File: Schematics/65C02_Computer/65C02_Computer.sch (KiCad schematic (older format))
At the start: 33 parts

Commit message: Various updates to schematic
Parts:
- added unit 5 of U1
- added unit 5 of U4
- added unit 3 of U5
- J2: renamed from J?; value Conn_02x16_Top_Bottom -> Expansion port; symbol Connector_Generic:Conn_02x16_Top_Bottom -> Connector_Generic:Conn_02x16_Odd_Even
- U4: renamed from U?; footprint (none) -> Package_DIP:DIP-14_W7.62mm_Socket
- gave numbers to parts that had none: 29
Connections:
- net +5V: now also U1.14 (VCC), U4.14 (VCC), U5.14 (VCC)
- net CLK: now also J2.18 (Pin_18); no longer J2.25 (Pin_25)
- net GND: now also J2.30 (Pin_30), U1.7 (GND), U4.7 (GND), U5.7 (GND); no longer J2.31 (Pin_31)
- net R~W: now also J2.20 (Pin_20); no longer J2.26 (Pin_26)
- net a1: now also J2.3 (Pin_3); no longer J2.2 (Pin_2)
- net a10: now also J2.21 (Pin_21); no longer J2.11 (Pin_11)
- net a11: now also J2.23 (Pin_23); no longer J2.12 (Pin_12)
- net a12: now also J2.25 (Pin_25); no longer J2.13 (Pin_13)
- net a13: now also J2.27 (Pin_27); no longer J2.14 (Pin_14)
- net a14: now also J2.29 (Pin_29); no longer J2.15 (Pin_15)
- net a15: now also J2.31 (Pin_31); no longer J2.16 (Pin_16)
- net a2: now also J2.5 (Pin_5); no longer J2.3 (Pin_3)
- net a3: now also J2.7 (Pin_7); no longer J2.4 (Pin_4)
- net a4: now also J2.9 (Pin_9); no longer J2.5 (Pin_5)
- net a5: now also J2.11 (Pin_11); no longer J2.6 (Pin_6)
- net a6: now also J2.13 (Pin_13); no longer J2.7 (Pin_7)
- net a7: now also J2.15 (Pin_15); no longer J2.8 (Pin_8)
- net a8: now also J2.17 (Pin_17); no longer J2.9 (Pin_9)
- net a9: now also J2.19 (Pin_19); no longer J2.10 (Pin_10)
- net d0: now also J2.2 (Pin_2); no longer J2.17 (Pin_17)
- net d1: now also J2.4 (Pin_4); no longer J2.18 (Pin_18)
- net d2: now also J2.6 (Pin_6); no longer J2.19 (Pin_19)
- net d3: now also J2.8 (Pin_8); no longer J2.20 (Pin_20)
- net d4: now also J2.10 (Pin_10); no longer J2.21 (Pin_21)
- net d5: now also J2.12 (Pin_12); no longer J2.22 (Pin_22)
- net d6: now also J2.14 (Pin_14); no longer J2.23 (Pin_23)
- net d7: now also J2.16 (Pin_16); no longer J2.24 (Pin_24)
- net ~IOCS: now also J2.22 (Pin_22); no longer J2.27 (Pin_27)
- net ~IRQX: now also J2.26 (Pin_26); no longer J2.29 (Pin_29)
- net ~RES: now also J2.24 (Pin_24); no longer J2.28 (Pin_28)
- no-connect marks 6 -> 7

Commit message: Further updates to schematic
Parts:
- added R13: 4K7, Resistor_THT:R_Axial_DIN0207_L6.3mm_D2.5mm_P7.62mm_Horizontal, symbol Device:R
- R1, R2, R4: value 3K3 -> 4K7
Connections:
- net +5V: now also R13.1
- net ~AIRQ: now also R13.2
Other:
- moved on the sheet: R4, U5A
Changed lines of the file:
@@
 P 1000 1600
 F 0 "R2" V 900 1600 50  0000 C CNN
-F 1 "3K3" V 1000 1600 50  0000 C CNN
+F 1 "4K7" V 1000 1600 50  0000 C CNN
 F 2 "Resistor_THT:R_Axial_DIN0207_L6.3mm_D2.5mm_P7.62mm_Horizontal" V 930 1600 50  0001 C CNN
 F 3 "~" H 1000 1600 50  0001 C CNN
@@
 P 1000 1200
 F 0 "R1" V 900 1200 50  0000 C CNN
-F 1 "3K3" V 1000 1200 50  0000 C CNN
+F 1 "4K7" V 1000 1200 50  0000 C CNN
 F 2 "Resistor_THT:R_Axial_DIN0207_L6.3mm_D2.5mm_P7.62mm_Horizontal" V 930 1200 50  0001 C CNN
 F 3 "~" H 1000 1200 50  0001 C CNN
@@
 L 74xx:74LS21 U5
 U 1 1 5E23A6D1
-P 8450 5300
-F 0 "U5" H 8450 5675 50  0000 C CNN
-F 1 "74HC21" H 8450 5584 50  0000 C CNN
-F 2 "Package_DIP:DIP-14_W7.62mm_Socket" H 8450 5300 50  0001 C CNN
-F 3 "http://www.ti.com/lit/gpn/sn74LS21" H 8450 5300 50  0001 C CNN
-	1    8450 5300
-	1    0    0    -1
-$EndComp
-Text GLabel 8050 5050 1    50   Input ~ 0
+P 9000 5400
+F 0 "U5" H 9000 5775 50  0000 C CNN
+F 1 "74HC21" H 9000 5684 50  0000 C CNN
+F 2 "Package_DIP:DIP-14_W7.62mm_Socket" H 9000 5400 50  0001 C CNN
+F 3 "http://www.ti.com/lit/gpn/sn74LS21" H 9000 5400 50  0001 C CNN
+	1    9000 5400
+	1    0    0    -1
+$EndComp
+Text GLabel 8600 5050 1    50   Input ~ 0
 ~V1IRQ
-Text GLabel 7900 5050 1    50   Input ~ 0
+Text GLabel 8450 5050 1    50   Input ~ 0
 ~V2IRQ
-Text GLabel 7750 5050 1    50   Input ~ 0
+Text GLabel 8300 5050 1    50   Input ~ 0
 ~AIRQ
 Wire Wire Line
-	8050 5050 8050 5150
-Wire Wire Line
-	8050 5150 8150 5150
-Wire Wire Line
-	7900 5050 7900 5250
-Wire Wire Line
-	7900 5250 8150 5250
-Wire Wire Line
-	7750 5050 7750 5350
-Wire Wire Line
-	7750 5350 8150 5350
-Wire Wire Line
-	7600 5050 7600 5450
-Wire Wire Line
-	7600 5450 8150 5450
-Text GLabel 8850 5300 2    50   Output ~ 0
+	8600 5050 8600 5250
+Wire Wire Line
+	8600 5250 8700 5250
+Wire Wire Line
+	8450 5050 8450 5350
+Wire Wire Line
+	8450 5350 8700 5350
+Wire Wire Line
+	8300 5050 8300 5450
+Wire Wire Line
+	8300 5450 8700 5450
+Wire Wire Line
+	8000 5050 8000 5550
+Text GLabel 9400 5400 2    50   Output ~ 0
 ~IRQ
 Wire Wire Line
-	8750 5300 8850 5300
+	9300 5400 9400 5400
 Wire Wire Line
 	2300 1300 2850 1300
@@
 Wire Wire Line
 	7150 5550 7150 5050
-Text GLabel 7600 5050 1    50   Input ~ 0
+Text GLabel 8000 5050 1    50   Input ~ 0
 ~IRQX
-Text GLabel 7450 5050 1    50   Input ~ 0
+Text GLabel 7850 5050 1    50   Input ~ 0
 +5V
 $Comp
 L Device:R R4
 U 1 1 5E451554
-P 7450 5300
-F 0 "R4" V 7350 5300 50  0000 C CNN
-F 1 "3K3" V 7450 5300 50  0000 C CNN
-F 2 "Resistor_THT:R_Axial_DIN0207_L6.3mm_D2.5mm_P7.62mm_Horizontal" V 7380 5300 50  0001 C CNN
-F 3 "~" H 7450 5300 50  0001 C CNN
-	1    7450 5300
-	1    0    0    -1
-$EndComp
-Wire Wire Line
-	7450 5050 7450 5150
-Wire Wire Line
-	7450 5450 7600 5450
-Connection ~ 7600 5450
+P 7850 5300
+F 0 "R4" V 7750 5300 50  0000 C CNN
+F 1 "4K7" V 7850 5300 50  0000 C CNN
+F 2 "Resistor_THT:R_Axial_DIN0207_L6.3mm_D2.5mm_P7.62mm_Horizontal" V 7780 5300 50  0001 C CNN
+F 3 "~" H 7850 5300 50  0001 C CNN
+	1    7850 5300
+	1    0    0    -1
+$EndComp
+Wire Wire Line
+	7850 5050 7850 5150
 $Comp
 L Connector:Conn_01x02_Male J1
@@
 Wire Wire Line
 	2850 6350 2850 6250
+Text GLabel 8150 5050 1    50   Input ~ 0
++5V
+$Comp
+L Device:R R13
+U 1 1 5E47EC64
+P 8150 5300
+F 0 "R13" V 8050 5300 50  0000 C CNN
+F 1 "4K7" V 8150 5300 50  0000 C CNN
+F 2 "Resistor_THT:R_Axial_DIN0207_L6.3mm_D2.5mm_P7.62mm_Horizontal" V 8080 5300 50  0001 C CNN
+F 3 "~" H 8150 5300 50  0001 C CNN
+	1    8150 5300
+	1    0    0    -1
+$EndComp
+Wire Wire Line
+	8150 5050 8150 5150
+Wire Wire Line
+	8000 5550 8700 5550
+Wire Wire Line
+	7850 5450 7850 5550
+Wire Wire Line
+	7850 5550 8000 5550
+Connection ~ 8000 5550
+Wire Wire Line
+	8150 5450 8300 5450
+Connection ~ 8300 5450
 Wire Bus Line
 	3100 5450 3100 5650

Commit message: Reordered PCB components
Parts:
- J1: footprint Connector_PinHeader_2.54mm:PinHeader_1x02_P2.54mm_Vertical -> Connector_PinHeader_2.54mm:PinHeader_1x03_P2.54mm_Vertical; symbol Connector:Conn_01x02_Male -> Connector:Conn_01x03_Male
- renumbered C9 to C1, C1 to C11, C3 to C12, C5 to C13, C7 to C14, C11 to C15, C12 to C16, C6 to C2, C13 to C3, C2 to C5, C8 to C6, C10 to C7, R3 to R1, R4 to R13, R5 to R2, R6 to R3, R13 to R6, R1 to R7, R2 to R8, U5 to U1, U4 to U2, U1 to U3, U7 to U4, U3 to U7, U2 to U8, U6 to U9
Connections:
- net CLK: now also J1.2 (Pin_2); no longer J1.1 (Pin_1)
- net CLKOUT: now also J1.3 (Pin_3); no longer J1.2 (Pin_2)
- net GND: now also J1.1 (Pin_1)
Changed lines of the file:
@@
 	4400 1300 4500 1300
 $Comp
-L 74xx:74HC02 U1
+L 74xx:74HC02 U3
 U 2 1 5E1744DD
 P 4000 2000
-F 0 "U1" H 4000 2325 50  0000 C CNN
+F 0 "U3" H 4000 2325 50  0000 C CNN
 F 1 "74HC02" H 4000 2234 50  0000 C CNN
 F 2 "Package_DIP:DIP-14_W7.62mm_Socket" H 4000 2000 50  0001 C CNN
@@
 $EndComp
 $Comp
-L 74xx:74HC00 U4
+L 74xx:74HC00 U2
 U 3 1 5E171DC1
 P 4800 2100
-F 0 "U4" H 4800 2425 50  0000 C CNN
+F 0 "U2" H 4800 2425 50  0000 C CNN
 F 1 "74HC00" H 4800 2334 50  0000 C CNN
 F 2 "Package_DIP:DIP-14_W7.62mm_Socket" H 4800 2100 50  0001 C CNN
@@
 $EndComp
 $Comp
-L 74xx:74HC00 U4
+L 74xx:74HC00 U2
 U 2 1 5E16FD0A
 P 4800 1400
-F 0 "U4" H 4800 1725 50  0000 C CNN
+F 0 "U2" H 4800 1725 50  0000 C CNN
 F 1 "74HC00" H 4800 1634 50  0000 C CNN
 F 2 "Package_DIP:DIP-14_W7.62mm_Socket" H 4800 1400 50  0001 C CNN
@@
 $EndComp
 $Comp
-L 74xx:74HC00 U4
+L 74xx:74HC00 U2
 U 1 1 5E16D50B
 P 4000 1300
-F 0 "U4" H 4000 1625 50  0000 C CNN
+F 0 "U2" H 4000 1625 50  0000 C CNN
 F 1 "74HC00" H 4000 1534 50  0000 C CNN
 F 2 "Package_DIP:DIP-14_W7.62mm_Socket" H 4000 1300 50  0001 C CNN
@@
 $EndComp
 $Comp
-L Device:C C13
+L Device:C C3
 U 1 1 5E15B54A
 P 10150 3350
-F 0 "C13" H 10265 3396 50  0000 L CNN
+F 0 "C3" H 10265 3396 50  0000 L CNN
 F 1 "0.1uF" H 10265 3305 50  0000 L CNN
 F 2 "Capacitor_THT:C_Disc_D3.4mm_W2.1mm_P2.50mm" H 10188 3200 50  0001 C CNN
@@
 $EndComp
 $Comp
-L Device:R R2
+L Device:R R8
 U 1 1 5E14ABB7
 P 1000 1600
-F 0 "R2" V 900 1600 50  0000 C CNN
+F 0 "R8" V 900 1600 50  0000 C CNN
 F 1 "4K7" V 1000 1600 50  0000 C CNN
 F 2 "Resistor_THT:R_Axial_DIN0207_L6.3mm_D2.5mm_P7.62mm_Horizontal" V 930 1600 50  0001 C CNN
@@
 $EndComp
 $Comp
-L Device:R R1
+L Device:R R7
 U 1 1 5E14A45B
 P 1000 1200
-F 0 "R1" V 900 1200 50  0000 C CNN
+F 0 "R7" V 900 1200 50  0000 C CNN
 F 1 "4K7" V 1000 1200 50  0000 C CNN
 F 2 "Resistor_THT:R_Axial_DIN0207_L6.3mm_D2.5mm_P7.62mm_Horizontal" V 930 1200 50  0001 C CNN
@@
 $EndComp
 $Comp
-L 6502:65C02S U3
+L 6502:65C02S U7
 U 1 1 5E135500
 P 1800 2000
-F 0 "U3" H 1800 3150 50  0000 C CNN
+F 0 "U7" H 1800 3150 50  0000 C CNN
 F 1 "65C02S" H 1800 3050 50  0000 C CNN
 F 2 "Package_DIP:DIP-40_W15.24mm_Socket" H 1650 2950 50  0001 C CNN
@@
 $EndComp
 $Comp
-L 6502:28C256 U2
+L 6502:28C256 U8
 U 1 1 5E3D4005
 P 1550 5000
-F 0 "U2" H 1550 5915 50  0000 C CNN
+F 0 "U8" H 1550 5915 50  0000 C CNN
 F 1 "28C256" H 1550 5824 50  0000 C CNN
 F 2 "Package_DIP:DIP-28_W15.24mm_Socket" H 1500 5800 50  0001 C CNN
@@
 	2600 5050 2700 5150
 $Comp
-L 6502:62256 U6
+L 6502:62256 U9
 U 1 1 5E37B16A
 P 3850 5000
-F 0 "U6" H 3850 5915 50  0000 C CNN
+F 0 "U9" H 3850 5915 50  0000 C CNN
 F 1 "62256" H 3850 5824 50  0000 C CNN
 F 2 "Package_DIP:DIP-28_W15.24mm_Socket" H 3800 5800 50  0001 C CNN
@@
 	4350 4450 4600 4450
 $Comp
-L Timer:NE555 U7
+L Timer:NE555 U4
 U 1 1 5E17C676
 P 7450 1700
-F 0 "U7" H 7450 1750 50  0000 C CNN
+F 0 "U4" H 7450 1750 50  0000 C CNN
 F 1 "NE555" H 7450 1650 50  0000 C CNN
 F 2 "Package_DIP:DIP-8_W7.62mm_Socket" H 7450 1700 50  0001 C CNN
@@
 	8050 1900 7950 1900
 $Comp
-L Device:R R5
+L Device:R R2
 U 1 1 5E1F5B26
 P 8050 1250
-F 0 "R5" V 7950 1250 50  0000 C CNN
+F 0 "R2" V 7950 1250 50  0000 C CNN
 F 1 "47K" V 8050 1250 50  0000 C CNN
 F 2 "Resistor_THT:R_Axial_DIN0207_L6.3mm_D2.5mm_P7.62mm_Horizontal" V 7980 1250 50  0001 C CNN
@@
 $EndComp
 $Comp
-L Device:CP C8
+L Device:CP C6
 U 1 1 5E2337BD
 P 8050 2150
-F 0 "C8" H 8168 2196 50  0000 L CNN
+F 0 "C6" H 8168 2196 50  0000 L CNN
 F 1 "10uF" H 8168 2105 50  0000 L CNN
 F 2 "Capacitor_THT:CP_Radial_D5.0mm_P2.50mm" H 8088 2000 50  0001 C CNN
@@
 Connection ~ 6700 1500
 $Comp
-L Device:R R3
+L Device:R R1
 U 1 1 5E3A85D8
 P 6700 1250
-F 0 "R3" V 6600 1250 50  0000 C CNN
+F 0 "R1" V 6600 1250 50  0000 C CNN
 F 1 "1M" V 6700 1250 50  0000 C CNN
 F 2 "Resistor_THT:R_Axial_DIN0207_L6.3mm_D2.5mm_P7.62mm_Horizontal" V 6630 1250 50  0001 C CNN
@@
 	8850 1500 8950 1500
 $Comp
-L Device:R R6
+L Device:R R3
 U 1 1 5E552FBE
 P 8950 1250
-F 0 "R6" V 8850 1250 50  0000 C CNN
+F 0 "R3" V 8850 1250 50  0000 C CNN
 F 1 "1K" V 8950 1250 50  0000 C CNN
 F 2 "Resistor_THT:R_Axial_DIN0207_L6.3mm_D2.5mm_P7.62mm_Horizontal" V 8880 1250 50  0001 C CNN
@@
 GND
 $Comp
-L Device:C C2
+L Device:C C5
 U 1 1 5E7C431C
 P 6150 1700
-F 0 "C2" H 6265 1746 50  0000 L CNN
+F 0 "C5" H 6265 1746 50  0000 L CNN
 F 1 "0.1uF" H 6265 1655 50  0000 L CNN
 F 2 "Capacitor_THT:C_Disc_D3.4mm_W2.1mm_P2.50mm" H 6188 1550 50  0001 C CNN
@@
 	2850 1500 2850 1300
 $Comp
-L 74xx:74HC00 U4
+L 74xx:74HC00 U2
 U 4 1 5E218D59
 P 8550 1500
-F 0 "U4" H 8550 1825 50  0000 C CNN
+F 0 "U2" H 8550 1825 50  0000 C CNN
 F 1 "74HC00" H 8550 1734 50  0000 C CNN
 F 2 "Package_DIP:DIP-14_W7.62mm_Socket" H 8550 1500 50  0001 C CNN
@@
 	8150 1500 8150 1600
 $Comp
-L 74xx:74LS21 U5
+L 74xx:74LS21 U1
 U 1 1 5E23A6D1
 P 9000 5400
-F 0 "U5" H 9000 5775 50  0000 C CNN
+F 0 "U1" H 9000 5775 50  0000 C CNN
 F 1 "74HC21" H 9000 5684 50  0000 C CNN
 F 2 "Package_DIP:DIP-14_W7.62mm_Socket" H 9000 5400 50  0001 C CNN
@@
 	2850 1300 2850 1000
 $Comp
-L Device:C C12
+L Device:C C16
 U 1 1 5E3E0FFB
 P 9700 3350
-F 0 "C12" H 9815 3396 50  0000 L CNN
+F 0 "C16" H 9815 3396 50  0000 L CNN
 F 1 "0.1uF" H 9815 3305 50  0000 L CNN
 F 2 "Capacitor_THT:C_Disc_D3.4mm_W2.1mm_P2.50mm" H 9738 3200 50  0001 C CNN
@@
 $EndComp
 $Comp
-L Device:C C11
+L Device:C C15
 U 1 1 5E3E14F5
 P 9250 3350
-F 0 "C11" H 9365 3396 50  0000 L CNN
+F 0 "C15" H 9365 3396 50  0000 L CNN
 F 1 "0.1uF" H 9365 3305 50  0000 L CNN
 F 2 "Capacitor_THT:C_Disc_D3.4mm_W2.1mm_P2.50mm" H 9288 3200 50  0001 C CNN
@@
 $EndComp
 $Comp
-L Device:C C10
+L Device:C C7
 U 1 1 5E3E1910
 P 8800 3350
-F 0 "C10" H 8915 3396 50  0000 L CNN
+F 0 "C7" H 8915 3396 50  0000 L CNN
 F 1 "0.1uF" H 8915 3305 50  0000 L CNN
 F 2 "Capacitor_THT:C_Disc_D3.4mm_W2.1mm_P2.50mm" H 8838 3200 50  0001 C CNN
@@
 $EndComp
 $Comp
-L Device:C C9
+L Device:C C1
 U 1 1 5E3E1BD5
 P 8350 3350
-F 0 "C9" H 8465 3396 50  0000 L CNN
+F 0 "C1" H 8465 3396 50  0000 L CNN
 F 1 "0.1uF" H 8465 3305 50  0000 L CNN
 F 2 "Capacitor_THT:C_Disc_D3.4mm_W2.1mm_P2.50mm" H 8388 3200 50  0001 C CNN
@@
 $EndComp
 $Comp
-L Device:C C7
+L Device:C C14
 U 1 1 5E3E1DA8
 P 7900 3350
-F 0 "C7" H 8015 3396 50  0000 L CNN
+F 0 "C14" H 8015 3396 50  0000 L CNN
 F 1 "0.1uF" H 8015 3305 50  0000 L CNN
 F 2 "Capacitor_THT:C_Disc_D3.4mm_W2.1mm_P2.50mm" H 7938 3200 50  0001 C CNN
@@
 $EndComp
 $Comp
-L Device:C C6
+L Device:C C2
 U 1 1 5E3E2103
 P 7450 3350
-F 0 "C6" H 7565 3396 50  0000 L CNN
+F 0 "C2" H 7565 3396 50  0000 L CNN
 F 1 "0.1uF" H 7565 3305 50  0000 L CNN
 F 2 "Capacitor_THT:C_Disc_D3.4mm_W2.1mm_P2.50mm" H 7488 3200 50  0001 C CNN
@@
 $EndComp
 $Comp
-L Device:C C5
+L Device:C C13
 U 1 1 5E3E2489
 P 7000 3350
-F 0 "C5" H 7115 3396 50  0000 L CNN
+F 0 "C13" H 7115 3396 50  0000 L CNN
 F 1 "0.1uF" H 7115 3305 50  0000 L CNN
 F 2 "Capacitor_THT:C_Disc_D3.4mm_W2.1mm_P2.50mm" H 7038 3200 50  0001 C CNN
@@
 Connection ~ 7000 3150
 $Comp
-L Device:C C3
+L Device:C C12
 U 1 1 5E6FCC42
 P 6550 3350
-F 0 "C3" H 6665 3396 50  0000 L CNN
+F 0 "C12" H 6665 3396 50  0000 L CNN
 F 1 "0.1uF" H 6665 3305 50  0000 L CNN
 F 2 "Capacitor_THT:C_Disc_D3.4mm_W2.1mm_P2.50mm" H 6588 3200 50  0001 C CNN
@@
 $EndComp
 $Comp
-L Device:C C1
+L Device:C C11
 U 1 1 5E6FCFF5
 P 6100 3350
-F 0 "C1" H 6215 3396 50  0000 L CNN
+F 0 "C11" H 6215 3396 50  0000 L CNN
 F 1 "0.1uF" H 6215 3305 50  0000 L CNN
 F 2 "Capacitor_THT:C_Disc_D3.4mm_W2.1mm_P2.50mm" H 6138 3200 50  0001 C CNN
@@
 +5V
 $Comp
-L Device:R R4
+L Device:R R13
 U 1 1 5E451554
 P 7850 5300
-F 0 "R4" V 7750 5300 50  0000 C CNN
+F 0 "R13" V 7750 5300 50  0000 C CNN
 F 1 "4K7" V 7850 5300 50  0000 C CNN
 F 2 "Resistor_THT:R_Axial_DIN0207_L6.3mm_D2.5mm_P7.62mm_Horizontal" V 7780 5300 50  0001 C CNN
@@
 	7850 5050 7850 5150
 $Comp
-L Connector:Conn_01x02_Male J1
+L Connector:Conn_01x03_Male J1
 U 1 1 5E49655D
 P 4400 2750
 F 0 "J1" H 4372 2632 50  0000 R CNN
 F 1 "CLK Jumper" H 4372 2723 50  0000 R CNN
-F 2 "Connector_PinHeader_2.54mm:PinHeader_1x02_P2.54mm_Vertical" H 4400 2750 50  0001 C CNN
+F 2 "Connector_PinHeader_2.54mm:PinHeader_1x03_P2.54mm_Vertical" H 4400 2750 50  0001 C CNN
 F 3 "~" H 4400 2750 50  0001 C CNN
 	1    4400 2750
@@
 	2700 2600 2600 2600
 $Comp
-L 74xx:74HC00 U4
+L 74xx:74HC00 U2
 U 5 1 5E5C6EF1
 P 2050 6850
-F 0 "U4" H 2280 6896 50  0000 L CNN
+F 0 "U2" H 2280 6896 50  0000 L CNN
 F 1 "74HC00" H 2280 6805 50  0000 L CNN
 F 2 "Package_DIP:DIP-14_W7.62mm_Socket" H 2050 6850 50  0001 C CNN
@@
 $EndComp
 $Comp
-L 74xx:74HC02 U1
+L 74xx:74HC02 U3
 U 5 1 5E5CBF34
 P 1250 6850
-F 0 "U1" H 1480 6896 50  0000 L CNN
+F 0 "U3" H 1480 6896 50  0000 L CNN
 F 1 "74HC02" H 1480 6805 50  0000 L CNN
 F 2 "Package_DIP:DIP-14_W7.62mm_Socket" H 1250 6850 50  0001 C CNN
@@
 $EndComp
 $Comp
-L 74xx:74LS21 U5
+L 74xx:74LS21 U1
 U 3 1 5E5E81AA
 P 2850 6850
-F 0 "U5" H 3080 6896 50  0000 L CNN
+F 0 "U1" H 3080 6896 50  0000 L CNN
 F 1 "74HC21" H 3080 6805 50  0000 L CNN
 F 2 "Package_DIP:DIP-14_W7.62mm_Socket" H 2850 6850 50  0001 C CNN
@@
 +5V
 $Comp
-L Device:R R13
+L Device:R R6
 U 1 1 5E47EC64
 P 8150 5300
-F 0 "R13" V 8050 5300 50  0000 C CNN
+F 0 "R6" V 8050 5300 50  0000 C CNN
 F 1 "4K7" V 8150 5300 50  0000 C CNN
 F 2 "Resistor_THT:R_Axial_DIN0207_L6.3mm_D2.5mm_P7.62mm_Horizontal" V 8080 5300 50  0001 C CNN
@@
 	8150 5450 8300 5450
 Connection ~ 8300 5450
+Text GLabel 4100 2850 0    50   Input ~ 0
+GND
+Wire Wire Line
+	4100 2850 4200 2850
 Wire Bus Line
 	3100 5450 3100 5650

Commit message: PCB RC1
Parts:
- renumbered J2 to J7
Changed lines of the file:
@@
 Sheet 1 2
 Title "65C02 Hobby Computer"
-Date "2020-02-03"
+Date "2020-02-17"
 Rev "v001"
 Comp ""
@@
 P 5850 5050
 AR Path="/5F14295C/6003736A" Ref="J?"  Part="1"
-AR Path="/6003736A" Ref="J2"  Part="1"
-F 0 "J2" H 5900 5967 50  0000 C CNN
+AR Path="/6003736A" Ref="J7"  Part="1"
+F 0 "J7" H 5900 5967 50  0000 C CNN
 F 1 "Expansion port" H 5900 5876 50  0000 C CNN
 F 2 "Connector_PinSocket_2.54mm:PinSocket_2x16_P2.54mm_Vertical" H 5850 5050 50  0001 C CNN

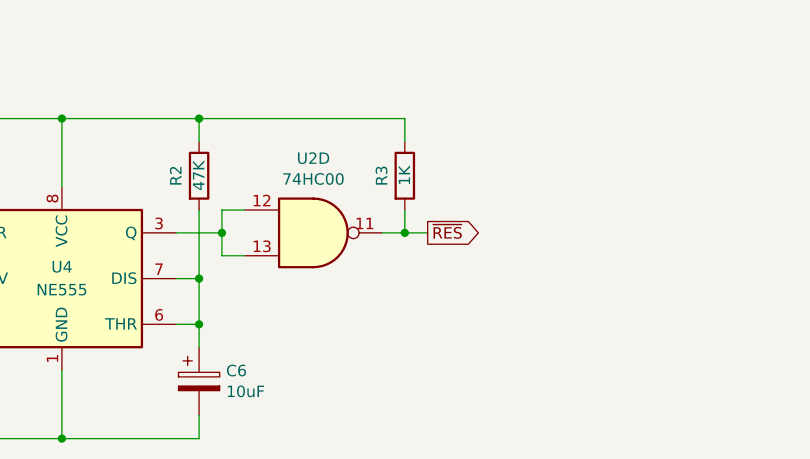
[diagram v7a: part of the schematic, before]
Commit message: Increased RESET pull-up resistor value
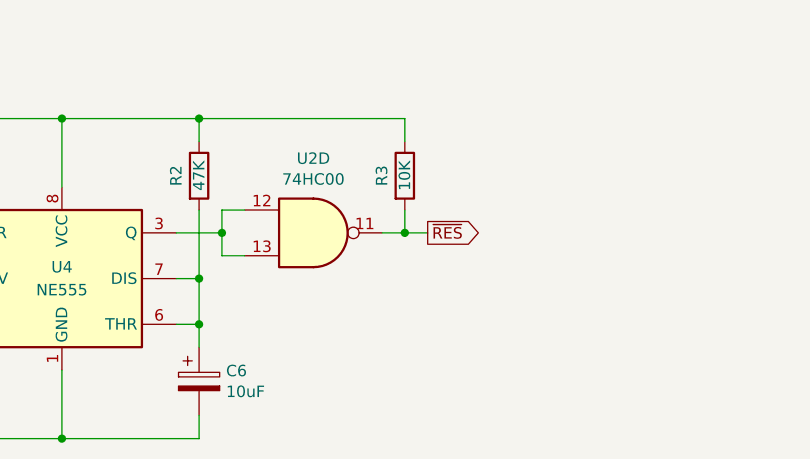
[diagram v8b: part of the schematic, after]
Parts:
- R3: value 1K -> 10K
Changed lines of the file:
@@
 P 8950 1250
 F 0 "R3" V 8850 1250 50  0000 C CNN
-F 1 "1K" V 8950 1250 50  0000 C CNN
+F 1 "10K" V 8950 1250 50  0000 C CNN
 F 2 "Resistor_THT:R_Axial_DIN0207_L6.3mm_D2.5mm_P7.62mm_Horizontal" V 8880 1250 50  0001 C CNN
 F 3 "~" H 8950 1250 50  0001 C CNN
